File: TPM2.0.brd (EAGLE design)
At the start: 25.9 x 32.4 mm, 7 parts

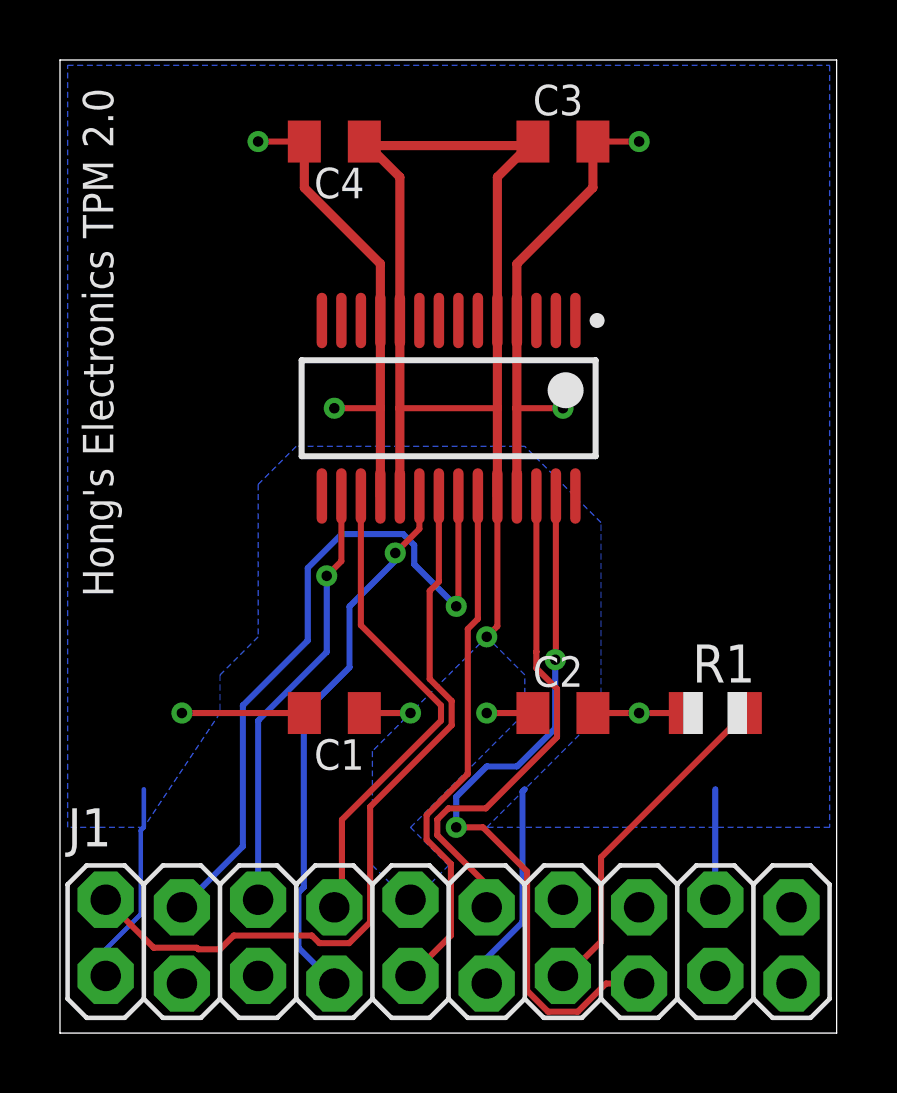
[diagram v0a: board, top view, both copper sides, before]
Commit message: Added more ground planes
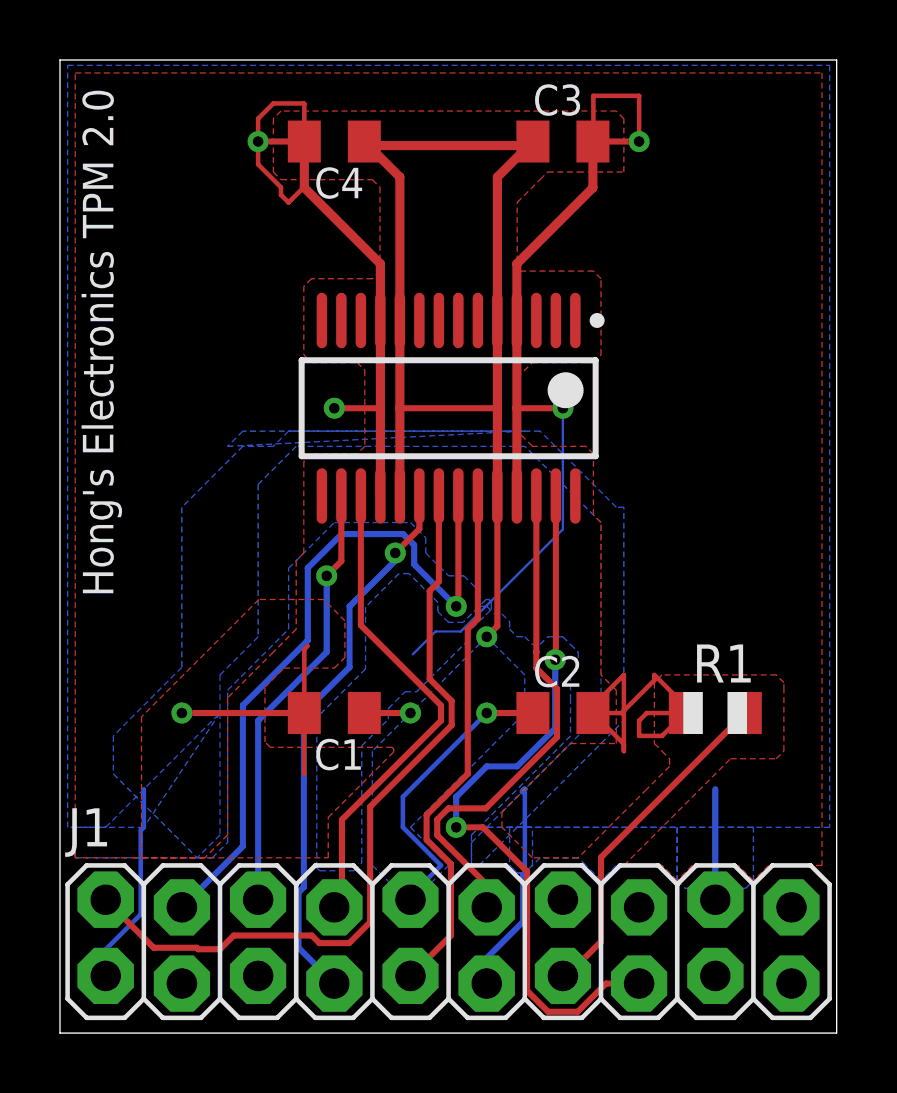
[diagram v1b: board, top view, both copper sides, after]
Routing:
- net GND: track 56.5 -> 96.9 mm, vias 6 -> 5
- net VCC: track 41.3 -> 49.7 mm
- added copper zone on layer 1, net GND
